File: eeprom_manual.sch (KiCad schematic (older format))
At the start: 45 parts, among them J1 Barrel_Jack, J2 Conn_01x02, SW1 SW_SPST, SW2 SW_DIP_x08, SW3 SW_DIP_x10, SW4 SW_DIP_x01, U1 L7805, U2 74HC245, U3 M54513FP, U4 28C16

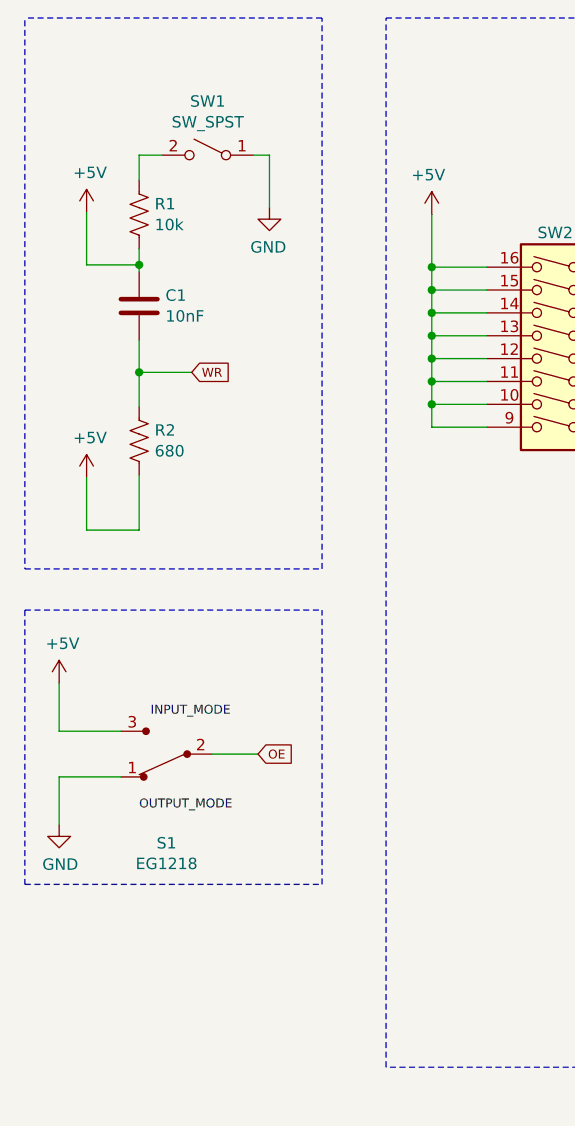
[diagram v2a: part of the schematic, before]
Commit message: Created pcbnew component layout
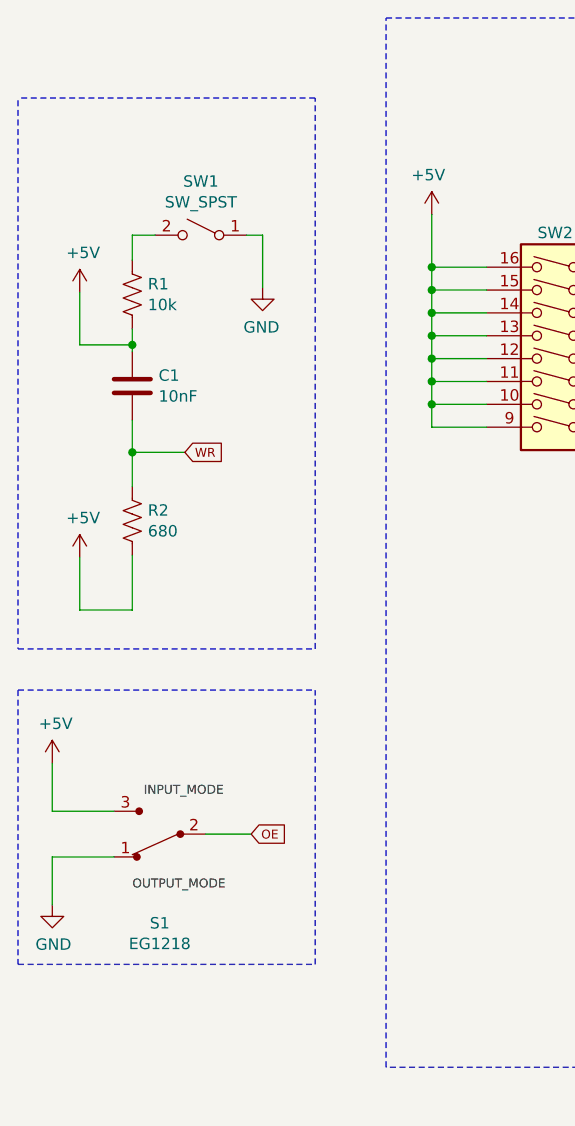
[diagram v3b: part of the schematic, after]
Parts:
- U1: footprint Package_TO_SOT_THT:TO-220-3_Horizontal_TabDown -> Package_TO_SOT_THT:TO-220-3_Vertical
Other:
- moved on the sheet: C1, R1, R2, S1, SW1
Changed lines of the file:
@@
 Wire Wire Line
 	7380 1370 7380 1170
-Text GLabel 1910 4100 2    39   Input ~ 0
+Text GLabel 1880 4450 2    39   Input ~ 0
 OE
 Wire Wire Line
-	1310 4000 1040 4000
-Wire Wire Line
-	1040 3790 1040 4000
+	1280 4350 1010 4350
+Wire Wire Line
+	1010 4140 1010 4350
 $Comp
 L dk_Slide_Switches:EG1218 S1
 U 1 1 5DA662DE
-P 1510 4100
-F 0 "S1" H 1510 4490 50  0000 C CNN
-F 1 "EG1218" H 1510 4580 50  0000 C CNN
-F 2 "digikey-footprints:Switch_Slide_11.6x4mm_EG1218" H 1710 4300 50  0001 L CNN
-F 3 "http://spec_sheets.e-switch.com/specs/P040040.pdf" H 1710 4400 60  0001 L CNN
-F 4 "EG1903-ND" H 1710 4500 60  0001 L CNN "Digi-Key_PN"
-F 5 "EG1218" H 1710 4600 60  0001 L CNN "MPN"
-F 6 "Switches" H 1710 4700 60  0001 L CNN "Category"
-F 7 "Slide Switches" H 1710 4800 60  0001 L CNN "Family"
-F 8 "http://spec_sheets.e-switch.com/specs/P040040.pdf" H 1710 4900 60  0001 L CNN "DK_Datasheet_Link"
-F 9 "/product-detail/en/e-switch/EG1218/EG1903-ND/101726" H 1710 5000 60  0001 L CNN "DK_Detail_Page"
-F 10 "SWITCH SLIDE SPDT 200MA 30V" H 1710 5100 60  0001 L CNN "Description"
-F 11 "E-Switch" H 1710 5200 60  0001 L CNN "Manufacturer"
-F 12 "Active" H 1710 5300 60  0001 L CNN "Status"
-	1    1510 4100
+P 1480 4450
+F 0 "S1" H 1480 4840 50  0000 C CNN
+F 1 "EG1218" H 1480 4930 50  0000 C CNN
+F 2 "digikey-footprints:Switch_Slide_11.6x4mm_EG1218" H 1680 4650 50  0001 L CNN
+F 3 "http://spec_sheets.e-switch.com/specs/P040040.pdf" H 1680 4750 60  0001 L CNN
+F 4 "EG1903-ND" H 1680 4850 60  0001 L CNN "Digi-Key_PN"
+F 5 "EG1218" H 1680 4950 60  0001 L CNN "MPN"
+F 6 "Switches" H 1680 5050 60  0001 L CNN "Category"
+F 7 "Slide Switches" H 1680 5150 60  0001 L CNN "Family"
+F 8 "http://spec_sheets.e-switch.com/specs/P040040.pdf" H 1680 5250 60  0001 L CNN "DK_Datasheet_Link"
+F 9 "/product-detail/en/e-switch/EG1218/EG1903-ND/101726" H 1680 5350 60  0001 L CNN "DK_Detail_Page"
+F 10 "SWITCH SLIDE SPDT 200MA 30V" H 1680 5450 60  0001 L CNN "Description"
+F 11 "E-Switch" H 1680 5550 60  0001 L CNN "Manufacturer"
+F 12 "Active" H 1680 5650 60  0001 L CNN "Status"
+	1    1480 4450
 	-1   0    0    1
 $EndComp
 Wire Wire Line
-	1310 4200 1040 4200
+	1280 4550 1010 4550
 $Comp
 L power:+5V #PWR01
 U 1 1 5DB5B091
-P 1040 3790
-F 0 "#PWR01" H 1040 3640 50  0001 C CNN
-F 1 "+5V" H 1055 3963 50  0000 C CNN
-F 2 "" H 1040 3790 50  0001 C CNN
-F 3 "" H 1040 3790 50  0001 C CNN
-	1    1040 3790
-	1    0    0    -1
-$EndComp
-Text Label 1390 4350 0    39   ~ 0
+P 1010 4140
+F 0 "#PWR01" H 1010 3990 50  0001 C CNN
+F 1 "+5V" H 1025 4313 50  0000 C CNN
+F 2 "" H 1010 4140 50  0001 C CNN
+F 3 "" H 1010 4140 50  0001 C CNN
+	1    1010 4140
+	1    0    0    -1
+$EndComp
+Text Label 1360 4700 0    39   ~ 0
 OUTPUT_MODE
-Text Label 1440 3940 0    39   ~ 0
+Text Label 1410 4290 0    39   ~ 0
 INPUT_MODE
 Wire Wire Line
-	1710 4100 1910 4100
+	1680 4450 1880 4450
 $Comp
 L power:GND #PWR02
 U 1 1 5DB2F7F2
-P 1040 4410
-F 0 "#PWR02" H 1040 4160 50  0001 C CNN
-F 1 "GND" H 1045 4237 50  0000 C CNN
-F 2 "" H 1040 4410 50  0001 C CNN
-F 3 "" H 1040 4410 50  0001 C CNN
-	1    1040 4410
-	1    0    0    -1
-$EndComp
-Wire Wire Line
-	1040 4410 1040 4200
+P 1010 4760
+F 0 "#PWR02" H 1010 4510 50  0001 C CNN
+F 1 "GND" H 1015 4587 50  0000 C CNN
+F 2 "" H 1010 4760 50  0001 C CNN
+F 3 "" H 1010 4760 50  0001 C CNN
+	1    1010 4760
+	1    0    0    -1
+$EndComp
+Wire Wire Line
+	1010 4760 1010 4550
 Wire Wire Line
 	7330 3150 7330 3220
@@
 L power:GND #PWR05
 U 1 1 5D8FA8CF
-P 1960 1710
-F 0 "#PWR05" H 1960 1460 50  0001 C CNN
-F 1 "GND" H 1965 1537 50  0000 C CNN
-F 2 "" H 1960 1710 50  0001 C CNN
-F 3 "" H 1960 1710 50  0001 C CNN
-	1    1960 1710
-	-1   0    0    -1
-$EndComp
-Wire Wire Line
-	1890 1480 1960 1480
-Wire Wire Line
-	1390 1480 1490 1480
+P 1930 2060
+F 0 "#PWR05" H 1930 1810 50  0001 C CNN
+F 1 "GND" H 1935 1887 50  0000 C CNN
+F 2 "" H 1930 2060 50  0001 C CNN
+F 3 "" H 1930 2060 50  0001 C CNN
+	1    1930 2060
+	-1   0    0    -1
+$EndComp
+Wire Wire Line
+	1860 1830 1930 1830
+Wire Wire Line
+	1360 1830 1460 1830
 $Comp
 L Switch:SW_SPST SW1
 U 1 1 5D6EFB46
-P 1690 1480
-F 0 "SW1" H 1690 1715 50  0000 C CNN
-F 1 "SW_SPST" H 1690 1624 50  0000 C CNN
-F 2 "Button_Switch_THT:SW_PUSH_6mm" H 1690 1480 50  0001 C CNN
-F 3 "~" H 1690 1480 50  0001 C CNN
-	1    1690 1480
-	-1   0    0    -1
-$EndComp
-Wire Wire Line
-	1390 2880 1390 3120
-Wire Wire Line
-	1390 2290 1390 2430
-Text GLabel 1620 2430 2    39   Input ~ 0
+P 1660 1830
+F 0 "SW1" H 1660 2065 50  0000 C CNN
+F 1 "SW_SPST" H 1660 1974 50  0000 C CNN
+F 2 "Button_Switch_THT:SW_PUSH_6mm" H 1660 1830 50  0001 C CNN
+F 3 "~" H 1660 1830 50  0001 C CNN
+	1    1660 1830
+	-1   0    0    -1
+$EndComp
+Wire Wire Line
+	1360 3230 1360 3470
+Wire Wire Line
+	1360 2640 1360 2780
+Text GLabel 1590 2780 2    39   Input ~ 0
 WR
 Wire Wire Line
-	1620 2430 1390 2430
-Connection ~ 1390 2430
-Wire Wire Line
-	1390 2430 1390 2580
-Wire Wire Line
-	1160 1960 1160 1730
+	1590 2780 1360 2780
+Connection ~ 1360 2780
+Wire Wire Line
+	1360 2780 1360 2930
+Wire Wire Line
+	1130 2310 1130 2080
 $Comp
 L power:+5V #PWR03
 U 1 1 5D936E74
-P 1160 1730
-F 0 "#PWR03" H 1160 1580 50  0001 C CNN
-F 1 "+5V" H 1175 1903 50  0000 C CNN
-F 2 "" H 1160 1730 50  0001 C CNN
-F 3 "" H 1160 1730 50  0001 C CNN
-	1    1160 1730
-	1    0    0    -1
-$EndComp
-Wire Wire Line
-	1390 1890 1390 1960
+P 1130 2080
+F 0 "#PWR03" H 1130 1930 50  0001 C CNN
+F 1 "+5V" H 1145 2253 50  0000 C CNN
+F 2 "" H 1130 2080 50  0001 C CNN
+F 3 "" H 1130 2080 50  0001 C CNN
+	1    1130 2080
+	1    0    0    -1
+$EndComp
+Wire Wire Line
+	1360 2240 1360 2310
 $Comp
 L Device:R_US R1
 U 1 1 5D77A214
-P 1390 1740
-F 0 "R1" H 1458 1786 50  0000 L CNN
-F 1 "10k" H 1458 1695 50  0000 L CNN
-F 2 "Resistor_SMD:R_0805_2012Metric_Pad1.15x1.40mm_HandSolder" V 1430 1730 50  0001 C CNN
-F 3 "~" H 1390 1740 50  0001 C CNN
-	1    1390 1740
+P 1360 2090
+F 0 "R1" H 1428 2136 50  0000 L CNN
+F 1 "10k" H 1428 2045 50  0000 L CNN
+F 2 "Resistor_SMD:R_0805_2012Metric_Pad1.15x1.40mm_HandSolder" V 1400 2080 50  0001 C CNN
+F 3 "~" H 1360 2090 50  0001 C CNN
+	1    1360 2090
 	1    0    0    -1
 $EndComp
@@
 L Device:R_US R2
 U 1 1 5D7930DA
-P 1390 2730
-F 0 "R2" H 1458 2776 50  0000 L CNN
-F 1 "680" H 1458 2685 50  0000 L CNN
-F 2 "Resistor_SMD:R_0805_2012Metric_Pad1.15x1.40mm_HandSolder" V 1430 2720 50  0001 C CNN
-F 3 "~" H 1390 2730 50  0001 C CNN
-	1    1390 2730
-	1    0    0    -1
-$EndComp
-Wire Wire Line
-	1390 1480 1390 1590
-Wire Wire Line
-	1960 1480 1960 1710
+P 1360 3080
+F 0 "R2" H 1428 3126 50  0000 L CNN
+F 1 "680" H 1428 3035 50  0000 L CNN
+F 2 "Resistor_SMD:R_0805_2012Metric_Pad1.15x1.40mm_HandSolder" V 1400 3070 50  0001 C CNN
+F 3 "~" H 1360 3080 50  0001 C CNN
+	1    1360 3080
+	1    0    0    -1
+$EndComp
+Wire Wire Line
+	1360 1830 1360 1940
+Wire Wire Line
+	1930 1830 1930 2060
 $Comp
 L Device:C C1
 U 1 1 5D8D3837
-P 1390 2140
-F 0 "C1" H 1505 2186 50  0000 L CNN
-F 1 "10nF" H 1505 2095 50  0000 L CNN
-F 2 "Capacitor_SMD:C_0805_2012Metric_Pad1.15x1.40mm_HandSolder" H 1428 1990 50  0001 C CNN
-F 3 "~" H 1390 2140 50  0001 C CNN
-	1    1390 2140
-	1    0    0    -1
-$EndComp
-Wire Wire Line
-	1160 1960 1390 1960
-Connection ~ 1390 1960
-Wire Wire Line
-	1390 1960 1390 1990
-Wire Wire Line
-	1160 3120 1160 2890
+P 1360 2490
+F 0 "C1" H 1475 2536 50  0000 L CNN
+F 1 "10nF" H 1475 2445 50  0000 L CNN
+F 2 "Capacitor_SMD:C_0805_2012Metric_Pad1.15x1.40mm_HandSolder" H 1398 2340 50  0001 C CNN
+F 3 "~" H 1360 2490 50  0001 C CNN
+	1    1360 2490
+	1    0    0    -1
+$EndComp
+Wire Wire Line
+	1130 2310 1360 2310
+Connection ~ 1360 2310
+Wire Wire Line
+	1360 2310 1360 2340
+Wire Wire Line
+	1130 3470 1130 3240
 $Comp
 L power:+5V #PWR04
 U 1 1 5D77298B
-P 1160 2890
-F 0 "#PWR04" H 1160 2740 50  0001 C CNN
-F 1 "+5V" H 1175 3063 50  0000 C CNN
-F 2 "" H 1160 2890 50  0001 C CNN
-F 3 "" H 1160 2890 50  0001 C CNN
-	1    1160 2890
-	1    0    0    -1
-$EndComp
-Wire Wire Line
-	1160 3120 1390 3120
+P 1130 3240
+F 0 "#PWR04" H 1130 3090 50  0001 C CNN
+F 1 "+5V" H 1145 3413 50  0000 C CNN
+F 2 "" H 1130 3240 50  0001 C CNN
+F 3 "" H 1130 3240 50  0001 C CNN
+	1    1130 3240
+	1    0    0    -1
+$EndComp
+Wire Wire Line
+	1130 3470 1360 3470
 $Comp
 L Switch:SW_DIP_x08 SW2
@@
 F 0 "U1" H 3940 6432 50  0000 C CNN
 F 1 "L7805" H 3940 6341 50  0000 C CNN
-F 2 "Package_TO_SOT_THT:TO-220-3_Horizontal_TabDown" H 3965 6040 50  0001 L CIN
+F 2 "Package_TO_SOT_THT:TO-220-3_Vertical" H 3965 6040 50  0001 L CIN
 F 3 "http://www.st.com/content/ccc/resource/technical/document/datasheet/41/4f/b3/b0/12/d4/47/88/CD00000444.pdf/files/CD00000444.pdf/jcr:content/translations/en.CD00000444.pdf" H 3940 6140 50  0001 C CNN
 	1    3940 6190
@@
 	1170 7250 1170 5850
 Wire Notes Line
-	890  890  890  3290
-Wire Notes Line
-	890  3290 2190 3290
-Wire Notes Line
-	2190 3290 2190 880
-Wire Notes Line
-	2190 880  900  880
+	860  1240 860  3640
+Wire Notes Line
+	860  3640 2160 3640
+Wire Notes Line
+	2160 3640 2160 1230
+Wire Notes Line
+	2160 1230 870  1230
 Wire Wire Line
 	8300 4660 8300 4950
@@
 	2470 880  10870 880
 Wire Notes Line
-	890  3470 2190 3470
-Wire Notes Line
-	890  3470 890  4670
-Wire Notes Line
-	890  4670 2190 4670
-Wire Notes Line
-	2190 4670 2190 3470
+	860  3820 2160 3820
+Wire Notes Line
+	860  3820 860  5020
+Wire Notes Line
+	860  5020 2160 5020
+Wire Notes Line
+	2160 5020 2160 3820
 Wire Wire Line
 	2280 6810 2280 6910

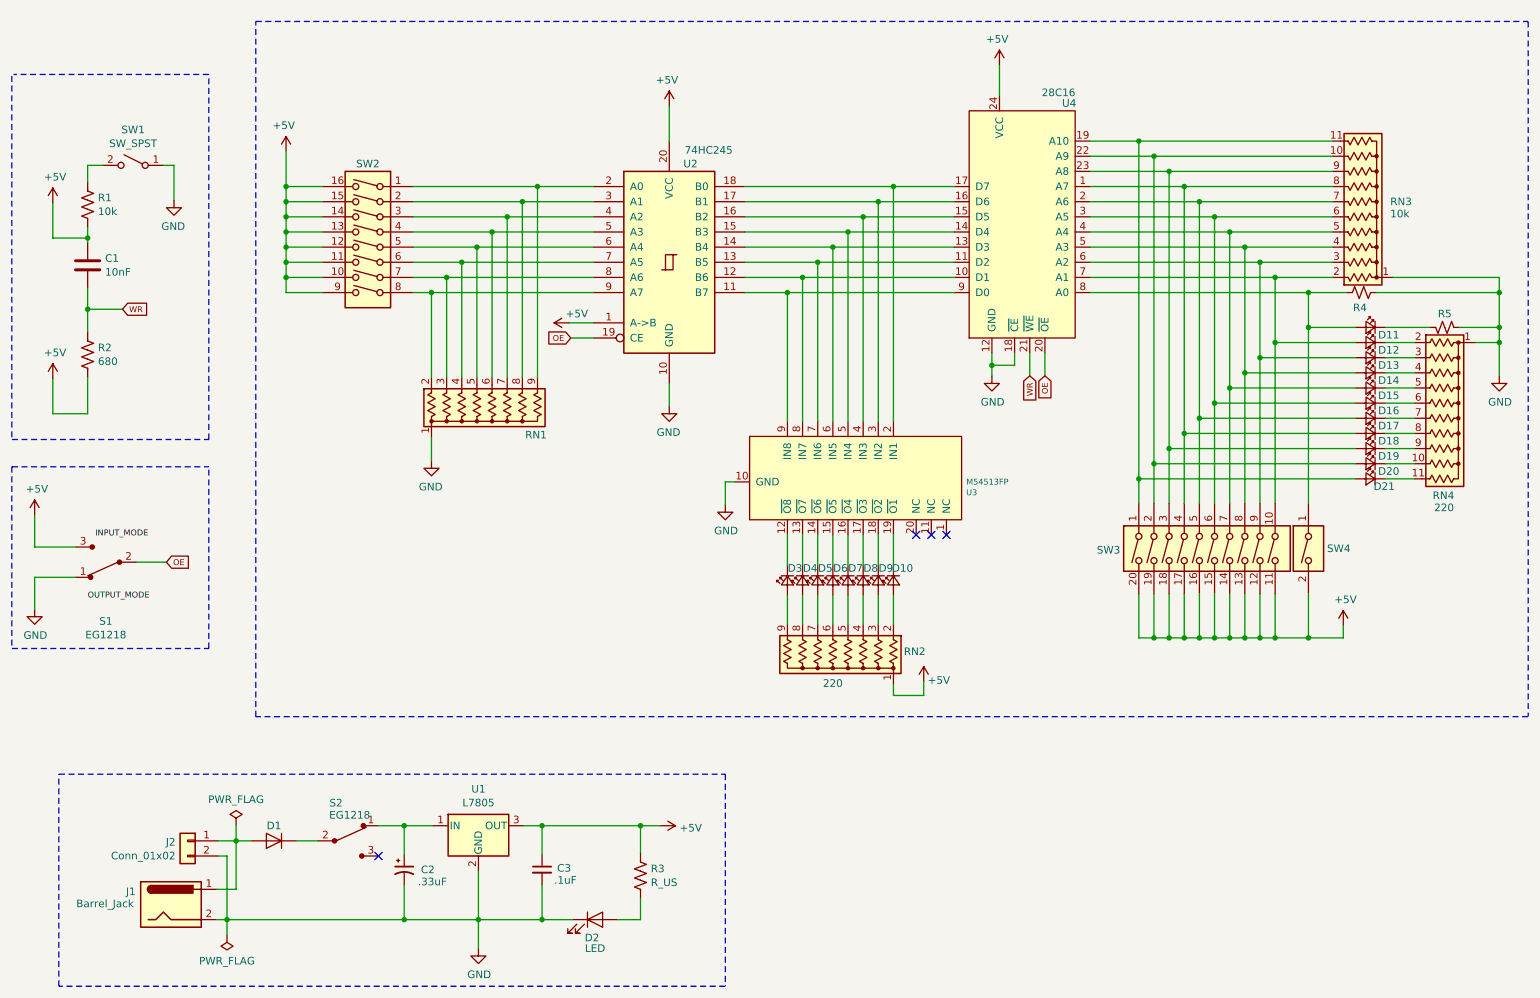
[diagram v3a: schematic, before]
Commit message: move from lm7805 to coin cell with boost converter +5v wall supply
- reorg single sheet sch to hierarchial kicad layout
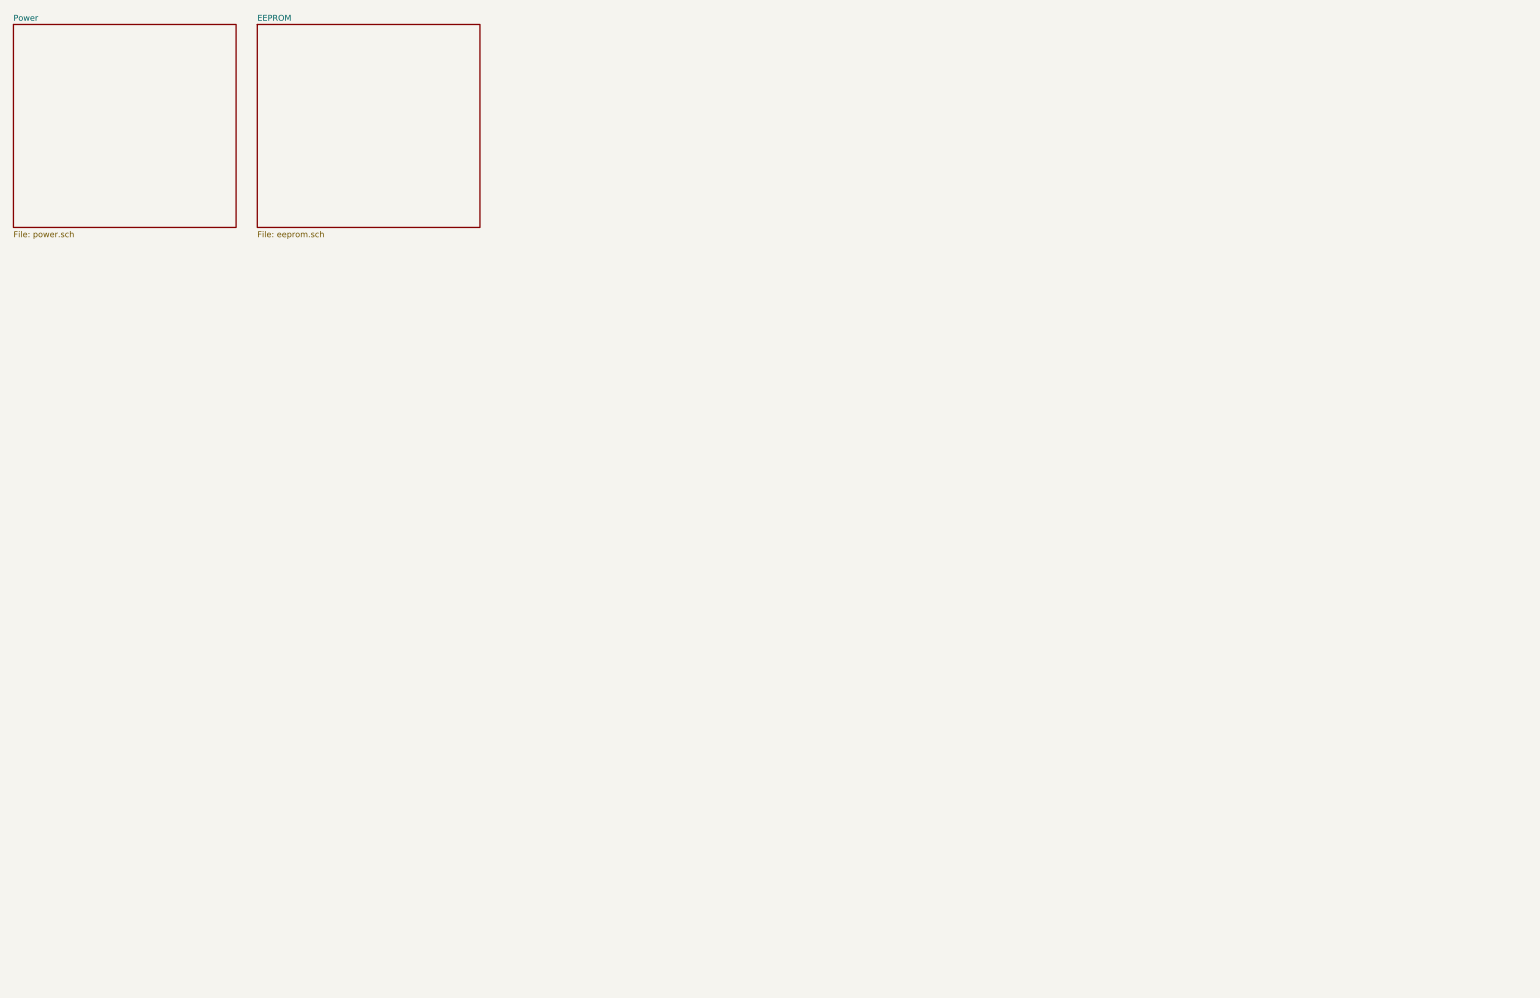
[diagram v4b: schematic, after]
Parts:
- removed C1: 10nF, Capacitor_SMD:C_0805_2012Metric_Pad1.15x1.40mm_HandSolder, symbol Device:C
- removed C2: .33uF, Capacitor_SMD:C_0805_2012Metric_Pad1.15x1.40mm_HandSolder, symbol Device:CP1_Small
- removed C3: .1uF, Capacitor_SMD:C_0805_2012Metric_Pad1.15x1.40mm_HandSolder, symbol Device:C_Small
- removed D1: D, Diode_SMD:D_0805_2012Metric_Pad1.15x1.40mm_HandSolder, symbol Device:D
- removed D10, D11, D12, D13, D14, D15, D16, D17, D18, D19, D20, D21, D3, D4, D5, D6, D7, D8, D9: RED, LED_SMD:LED_0805_2012Metric_Pad1.15x1.40mm_HandSolder, symbol Device:LED_Small
- removed D2: LED, LED_SMD:LED_0805_2012Metric_Pad1.15x1.40mm_HandSolder, symbol Device:LED
- removed J1: Barrel_Jack, digikey-footprints:Barrel_Jack_5.5mmODx2.1mmID_PJ-202A, symbol Connector:Barrel_Jack
- removed J2: Conn_01x02, TerminalBlock:TerminalBlock_bornier-2_P5.08mm, symbol Connector_Generic:Conn_01x02
- removed R1: 10k, Resistor_SMD:R_0805_2012Metric_Pad1.15x1.40mm_HandSolder, symbol Device:R_US
- removed R2: 680, Resistor_SMD:R_0805_2012Metric_Pad1.15x1.40mm_HandSolder, symbol Device:R_US
- removed R3: R_US, Resistor_SMD:R_0805_2012Metric_Pad1.15x1.40mm_HandSolder, symbol Device:R_US
- removed R4: 10k, Resistor_SMD:R_0805_2012Metric_Pad1.15x1.40mm_HandSolder, symbol Device:R_Small_US
- removed R5: 220, Resistor_SMD:R_0805_2012Metric_Pad1.15x1.40mm_HandSolder, symbol Device:R_Small_US
- removed RN1: R_VALUE, Resistor_THT:R_Array_SIP9, symbol Device:R_Network08_US
- removed RN2: 220, Resistor_THT:R_Array_SIP9, symbol Device:R_Network08_US
- removed RN3: 10k, Resistor_THT:R_Array_SIP11, symbol Device:R_Network10_US
- removed RN4: 220, Resistor_THT:R_Array_SIP11, symbol Device:R_Network10_US
- removed S1, S2: EG1218, digikey-footprints:Switch_Slide_11.6x4mm_EG1218, symbol dk_Slide_Switches:EG1218
- removed SW1: SW_SPST, Button_Switch_THT:SW_PUSH_6mm, symbol Switch:SW_SPST
- removed SW2: SW_DIP_x08, Button_Switch_THT:SW_DIP_SPSTx08_Slide_9.78x22.5mm_W7.62mm_P2.54mm, symbol Switch:SW_DIP_x08
- removed SW3: SW_DIP_x10, Button_Switch_THT:SW_DIP_SPSTx10_Slide_9.78x27.58mm_W7.62mm_P2.54mm, symbol Switch:SW_DIP_x10
- removed SW4: SW_DIP_x01, Button_Switch_THT:SW_DIP_SPSTx01_Slide_9.78x4.72mm_W7.62mm_P2.54mm, symbol Switch:SW_DIP_x01
- removed U1: L7805, Package_TO_SOT_THT:TO-220-3_Vertical, symbol Regulator_Linear:L7805
- removed U2: 74HC245, Package_SO:TSSOP-20_4.4x6.5mm_P0.65mm, symbol 74xx:74HC245
- removed U3: M54513FP, digikey-footprints:SSOP-20_W5.3mm, symbol eeprom_manual:M54513FP
- removed U4: 28C16, Socket:DIP_Socket-24_W11.9_W12.7_W15.24_W17.78_W18.5_3M_224-1275-00-0602J, symbol eeprom_manual:AT28C16
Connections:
- no-connect marks 4 -> 0
